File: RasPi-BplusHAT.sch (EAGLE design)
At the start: 1 part, among them K2 RASPI_HEADER

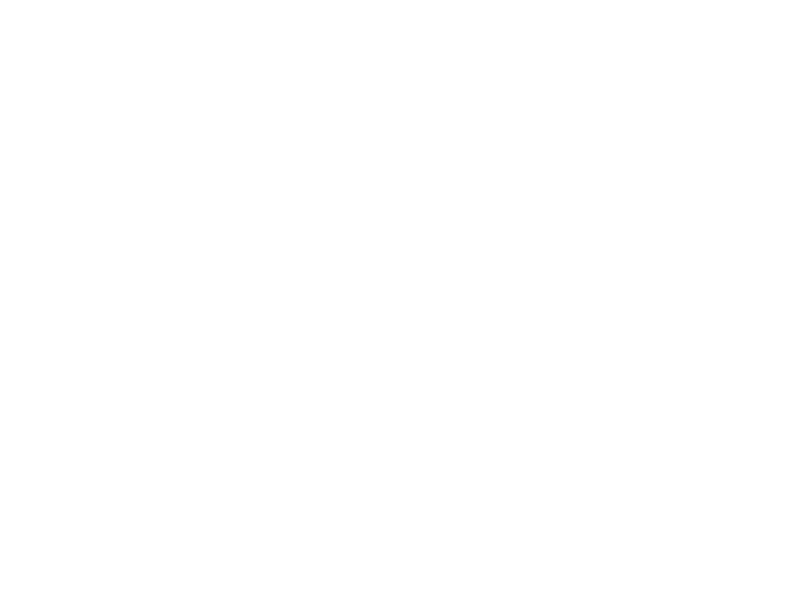
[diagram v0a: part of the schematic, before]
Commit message: add db15 and labeled nets
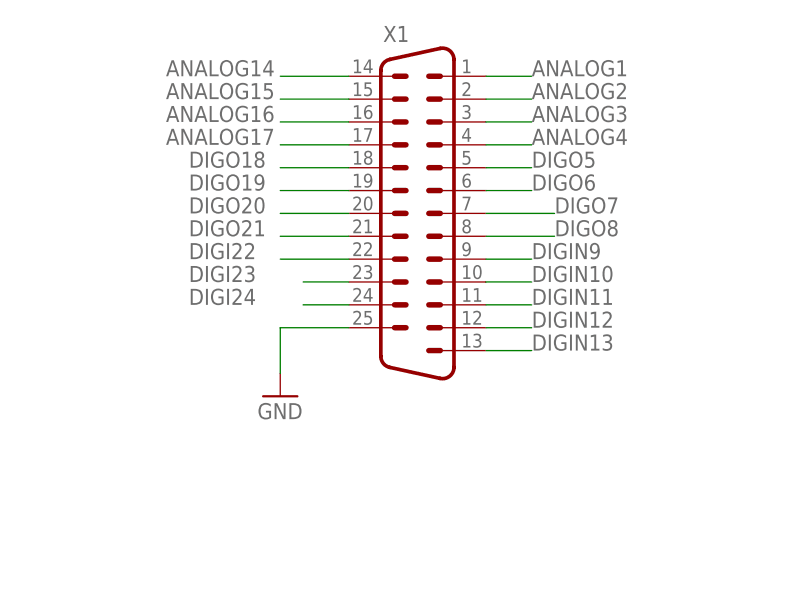
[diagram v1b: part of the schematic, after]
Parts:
- added X1: (no value), con-subd:M25HP
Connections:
- new net ANALOG1: X1G$1.1
- new net ANALOG14: X1G$1.14
- new net ANALOG15: X1G$1.15
- new net ANALOG16: X1G$1.16
- new net ANALOG17: X1G$1.17
- new net ANALOG2: X1G$1.2
- new net ANALOG3: X1G$1.3
- new net ANALOG4: X1G$1.4
- new net DIGI22: X1G$1.22
- new net DIGI23: X1G$1.23
- new net DIGI24: X1G$1.24
- new net DIGIN10: X1G$1.10
- new net DIGIN11: X1G$1.11
- new net DIGIN12: X1G$1.12
- new net DIGIN13: X1G$1.13
- new net DIGIN9: X1G$1.9
- new net DIGO18: X1G$1.18
- new net DIGO19: X1G$1.19
- new net DIGO20: X1G$1.20
- new net DIGO21: X1G$1.21
- new net DIGO5: X1G$1.5
- new net DIGO6: X1G$1.6
- new net DIGO7: X1G$1.7
- new net DIGO8: X1G$1.8
- net GND: now also X1G$1.25
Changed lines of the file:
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@@
 <part name="P+1" library="supply1" deviceset="+5V" device=""/>
 <part name="K2" library="RasPi-BplusHAT" deviceset="RASPI_HEADER" device=""/>
+<part name="X1" library="con-subd" deviceset="M25HP" device=""/>
+<part name="GND1" library="supply1" deviceset="GND" device=""/>
 </parts>
 <sheets>
@@
 </instance>
 <instance part="K2" gate="G$1" x="50.8" y="152.4" rot="R180"/>
+<instance part="X1" gate="G$1" x="177.8" y="187.96"/>
+<instance part="GND1" gate="1" x="162.56" y="165.1"/>
 </instances>
 <busses>
@@
 <pinref part="K2" gate="G$1" pin="34"/>
 </segment>
+<segment>
+<pinref part="X1" gate="G$1" pin="25"/>
+<wire x1="170.18" y1="172.72" x2="162.56" y2="172.72" width="0.1524" layer="91"/>
+<pinref part="GND1" gate="1" pin="GND"/>
+<wire x1="162.56" y1="172.72" x2="162.56" y2="167.64" width="0.1524" layer="91"/>
+</segment>
 </net>
 <net name="+3V3" class="0">
@@
 </segment>
 </net>
+<net name="ANALOG1" class="0">
+<segment>
+<pinref part="X1" gate="G$1" pin="1"/>
+<wire x1="185.42" y1="200.66" x2="190.5" y2="200.66" width="0.1524" layer="91"/>
+<label x="190.5" y="200.66" size="1.778" layer="95"/>
+</segment>
+</net>
+<net name="ANALOG2" class="0">
+<segment>
+<pinref part="X1" gate="G$1" pin="2"/>
+<wire x1="185.42" y1="198.12" x2="190.5" y2="198.12" width="0.1524" layer="91"/>
+<label x="190.5" y="198.12" size="1.778" layer="95"/>
+</segment>
+</net>
+<net name="ANALOG3" class="0">
+<segment>
+<pinref part="X1" gate="G$1" pin="3"/>
+<wire x1="185.42" y1="195.58" x2="190.5" y2="195.58" width="0.1524" layer="91"/>
+<label x="190.5" y="195.58" size="1.778" layer="95"/>
+</segment>
+</net>
+<net name="ANALOG4" class="0">
+<segment>
+<pinref part="X1" gate="G$1" pin="4"/>
+<wire x1="185.42" y1="193.04" x2="190.5" y2="193.04" width="0.1524" layer="91"/>
+<label x="190.5" y="193.04" size="1.778" layer="95"/>
+</segment>
+</net>
+<net name="DIGO5" class="0">
+<segment>
+<pinref part="X1" gate="G$1" pin="5"/>
+<wire x1="185.42" y1="190.5" x2="190.5" y2="190.5" width="0.1524" layer="91"/>
+<label x="190.5" y="190.5" size="1.778" layer="95"/>
+</segment>
+</net>
+<net name="DIGO6" class="0">
+<segment>
+<pinref part="X1" gate="G$1" pin="6"/>
+<wire x1="185.42" y1="187.96" x2="190.5" y2="187.96" width="0.1524" layer="91"/>
+<label x="190.5" y="187.96" size="1.778" layer="95"/>
+</segment>
+</net>
+<net name="DIGO7" class="0">
+<segment>
+<pinref part="X1" gate="G$1" pin="7"/>
+<wire x1="185.42" y1="185.42" x2="193.04" y2="185.42" width="0.1524" layer="91"/>
+<label x="193.04" y="185.42" size="1.778" layer="95"/>
+</segment>
+</net>
+<net name="DIGO8" class="0">
+<segment>
+<pinref part="X1" gate="G$1" pin="8"/>
+<wire x1="185.42" y1="182.88" x2="193.04" y2="182.88" width="0.1524" layer="91"/>
+<label x="193.04" y="182.88" size="1.778" layer="95"/>
+</segment>
+</net>
+<net name="DIGIN9" class="0">
+<segment>
+<pinref part="X1" gate="G$1" pin="9"/>
+<wire x1="185.42" y1="180.34" x2="190.5" y2="180.34" width="0.1524" layer="91"/>
+<label x="190.5" y="180.34" size="1.778" layer="95"/>
+</segment>
+</net>
+<net name="DIGIN10" class="0">
+<segment>
+<pinref part="X1" gate="G$1" pin="10"/>
+<wire x1="185.42" y1="177.8" x2="190.5" y2="177.8" width="0.1524" layer="91"/>
+<label x="190.5" y="177.8" size="1.778" layer="95"/>
+</segment>
+</net>
+<net name="DIGIN12" class="0">
+<segment>
+<pinref part="X1" gate="G$1" pin="12"/>
+<wire x1="185.42" y1="172.72" x2="190.5" y2="172.72" width="0.1524" layer="91"/>
+<label x="190.5" y="172.72" size="1.778" layer="95"/>
+</segment>
+</net>
+<net name="DIGIN13" class="0">
+<segment>
+<pinref part="X1" gate="G$1" pin="13"/>
+<wire x1="185.42" y1="170.18" x2="190.5" y2="170.18" width="0.1524" layer="91"/>
+<label x="190.5" y="170.18" size="1.778" layer="95"/>
+</segment>
+</net>
+<net name="ANALOG14" class="0">
+<segment>
+<pinref part="X1" gate="G$1" pin="14"/>
+<wire x1="170.18" y1="200.66" x2="162.56" y2="200.66" width="0.1524" layer="91"/>
+<label x="149.86" y="200.66" size="1.778" layer="95"/>
+</segment>
+</net>
+<net name="ANALOG15" class="0">
+<segment>
+<pinref part="X1" gate="G$1" pin="15"/>
+<wire x1="170.18" y1="198.12" x2="162.56" y2="198.12" width="0.1524" layer="91"/>
+<label x="149.86" y="198.12" size="1.778" layer="95"/>
+</segment>
+</net>
+<net name="ANALOG16" class="0">
+<segment>
+<pinref part="X1" gate="G$1" pin="16"/>
+<wire x1="170.18" y1="195.58" x2="162.56" y2="195.58" width="0.1524" layer="91"/>
+<label x="149.86" y="195.58" size="1.778" layer="95"/>
+</segment>
+</net>
+<net name="ANALOG17" class="0">
+<segment>
+<pinref part="X1" gate="G$1" pin="17"/>
+<wire x1="170.18" y1="193.04" x2="162.56" y2="193.04" width="0.1524" layer="91"/>
+<label x="149.86" y="193.04" size="1.778" layer="95"/>
+</segment>
+</net>
+<net name="DIGO18" class="0">
+<segment>
+<pinref part="X1" gate="G$1" pin="18"/>
+<wire x1="170.18" y1="190.5" x2="162.56" y2="190.5" width="0.1524" layer="91"/>
+<label x="152.4" y="190.5" size="1.778" layer="95"/>
+</segment>
+</net>
+<net name="DIGO19" class="0">
+<segment>
+<pinref part="X1" gate="G$1" pin="19"/>
+<wire x1="170.18" y1="187.96" x2="162.56" y2="187.96" width="0.1524" layer="91"/>
+<label x="152.4" y="187.96" size="1.778" layer="95"/>
+</segment>
+</net>
+<net name="DIGO20" class="0">
+<segment>
+<pinref part="X1" gate="G$1" pin="20"/>
+<wire x1="170.18" y1="185.42" x2="162.56" y2="185.42" width="0.1524" layer="91"/>
+<label x="152.4" y="185.42" size="1.778" layer="95"/>
+</segment>
+</net>
+<net name="DIGO21" class="0">
+<segment>
+<pinref part="X1" gate="G$1" pin="21"/>
+<wire x1="170.18" y1="182.88" x2="162.56" y2="182.88" width="0.1524" layer="91"/>
+<label x="152.4" y="182.88" size="1.778" layer="95"/>
+</segment>
+</net>
+<net name="DIGI22" class="0">
+<segment>
+<pinref part="X1" gate="G$1" pin="22"/>
+<wire x1="170.18" y1="180.34" x2="162.56" y2="180.34" width="0.1524" layer="91"/>
+<label x="152.4" y="180.34" size="1.778" layer="95"/>
+</segment>
+</net>
+<net name="DIGI23" class="0">
+<segment>
+<pinref part="X1" gate="G$1" pin="23"/>
+<wire x1="170.18" y1="177.8" x2="165.1" y2="177.8" width="0.1524" layer="91"/>
+<label x="152.4" y="177.8" size="1.778" layer="95"/>
+</segment>
+</net>
+<net name="DIGI24" class="0">
+<segment>
+<pinref part="X1" gate="G$1" pin="24"/>
+<wire x1="170.18" y1="175.26" x2="165.1" y2="175.26" width="0.1524" layer="91"/>
+<label x="152.4" y="175.26" size="1.778" layer="95"/>
+</segment>
+</net>
+<net name="DIGIN11" class="0">
+<segment>
+<pinref part="X1" gate="G$1" pin="11"/>
+<wire x1="185.42" y1="175.26" x2="190.5" y2="175.26" width="0.1524" layer="91"/>
+<label x="190.5" y="175.26" size="1.778" layer="95"/>
+</segment>
+</net>

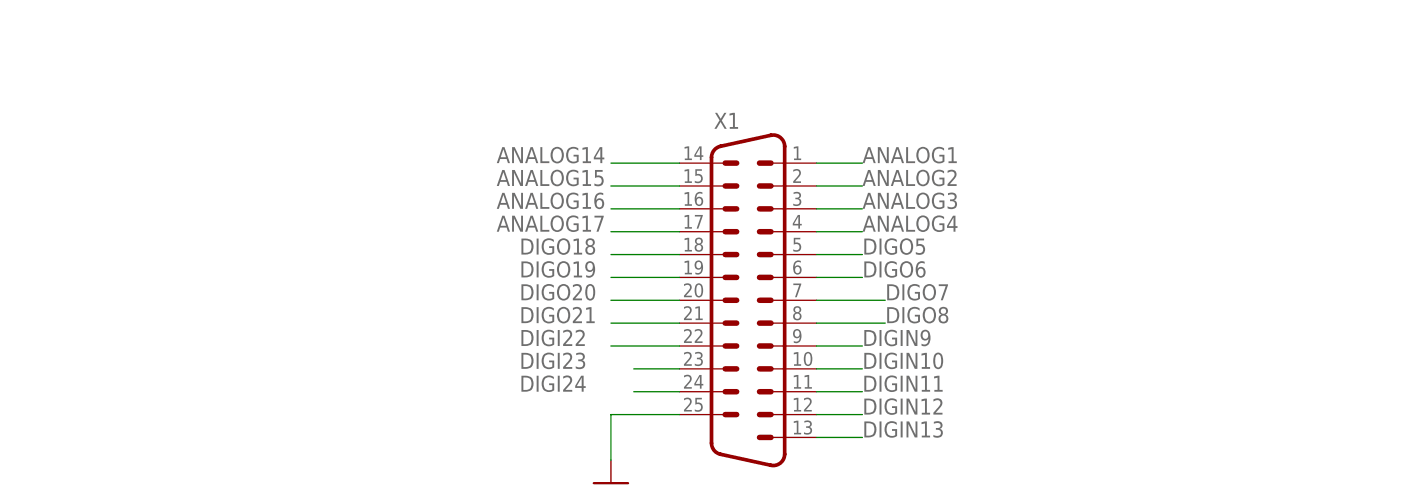
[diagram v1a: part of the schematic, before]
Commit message: add pullups
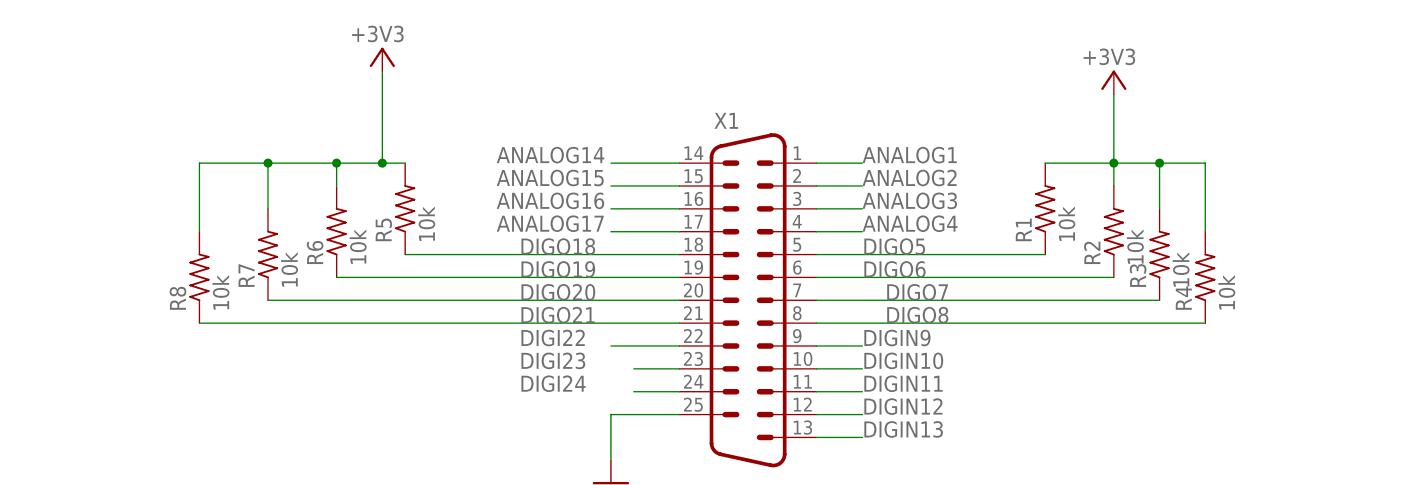
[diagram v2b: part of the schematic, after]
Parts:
- added R1, R2, R3, R4, R5, R6, R7, R8: 10k, resistor:R-US_0207/10
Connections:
- net +3V3: now also R1.2, R2.2, R3.2, R4.2, R5.2, R6.2, R7.2, R8.2
- net DIGO18: now also R5.1
- net DIGO19: now also R6.1
- net DIGO20: now also R7.1
- net DIGO21: now also R8.1
- net DIGO5: now also R1.1
- net DIGO6: now also R2.1
- net DIGO7: now also R3.1
- net DIGO8: now also R4.1
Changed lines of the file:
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@@
 <layer number="97" name="Info" color="7" fill="1" visible="yes" active="yes"/>
 <layer number="98" name="Guide" color="6" fill="1" visible="yes" active="yes"/>
+<layer number="99" name="SpiceOrder" color="5" fill="1" visible="yes" active="yes"/>
 <layer number="100" name="NonViaHole" color="7" fill="1" visible="yes" active="yes"/>
 <layer number="101" name="PlacementGuide" color="7" fill="1" visible="yes" active="yes"/>
@@
 <part name="X1" library="con-subd" deviceset="M25HP" device=""/>
 <part name="GND1" library="supply1" deviceset="GND" device=""/>
+<part name="+3V2" library="supply1" deviceset="+3V3" device=""/>
+<part name="R1" library="resistor" deviceset="R-US_" device="0207/10" value="10k"/>
+<part name="R2" library="resistor" deviceset="R-US_" device="0207/10" value="10k"/>
+<part name="R3" library="resistor" deviceset="R-US_" device="0207/10" value="10k"/>
+<part name="R4" library="resistor" deviceset="R-US_" device="0207/10" value="10k"/>
+<part name="+3V3" library="supply1" deviceset="+3V3" device=""/>
+<part name="R5" library="resistor" deviceset="R-US_" device="0207/10" value="10k"/>
+<part name="R6" library="resistor" deviceset="R-US_" device="0207/10" value="10k"/>
+<part name="R7" library="resistor" deviceset="R-US_" device="0207/10" value="10k"/>
+<part name="R8" library="resistor" deviceset="R-US_" device="0207/10" value="10k"/>
 </parts>
 <sheets>
@@
 <instance part="X1" gate="G$1" x="177.8" y="187.96"/>
 <instance part="GND1" gate="1" x="162.56" y="165.1"/>
+<instance part="+3V2" gate="G$1" x="218.44" y="210.82" smashed="yes">
+<attribute name="VALUE" x="220.98" y="213.36" size="1.778" layer="96" rot="R180"/>
+</instance>
+<instance part="R1" gate="G$1" x="210.82" y="195.58" rot="R90"/>
+<instance part="R2" gate="G$1" x="218.44" y="193.04" rot="R90"/>
+<instance part="R3" gate="G$1" x="223.52" y="190.5" rot="R90"/>
+<instance part="R4" gate="G$1" x="228.6" y="187.96" rot="R90"/>
+<instance part="+3V3" gate="G$1" x="137.16" y="213.36" smashed="yes">
+<attribute name="VALUE" x="139.7" y="215.9" size="1.778" layer="96" rot="R180"/>
+</instance>
+<instance part="R5" gate="G$1" x="139.7" y="195.58" rot="R90"/>
+<instance part="R6" gate="G$1" x="132.08" y="193.04" rot="R90"/>
+<instance part="R7" gate="G$1" x="124.46" y="190.5" rot="R90"/>
+<instance part="R8" gate="G$1" x="116.84" y="187.96" rot="R90"/>
 </instances>
 <busses>
@@
 <pinref part="K2" gate="G$1" pin="17"/>
 </segment>
+<segment>
+<pinref part="R1" gate="G$1" pin="2"/>
+<pinref part="+3V2" gate="G$1" pin="+3V3"/>
+<wire x1="210.82" y1="200.66" x2="218.44" y2="200.66" width="0.1524" layer="91"/>
+<wire x1="218.44" y1="200.66" x2="218.44" y2="208.28" width="0.1524" layer="91"/>
+<pinref part="R2" gate="G$1" pin="2"/>
+<wire x1="218.44" y1="198.12" x2="218.44" y2="200.66" width="0.1524" layer="91"/>
+<junction x="218.44" y="200.66"/>
+<pinref part="R3" gate="G$1" pin="2"/>
+<wire x1="218.44" y1="200.66" x2="223.52" y2="200.66" width="0.1524" layer="91"/>
+<wire x1="223.52" y1="200.66" x2="223.52" y2="195.58" width="0.1524" layer="91"/>
+<pinref part="R4" gate="G$1" pin="2"/>
+<wire x1="223.52" y1="200.66" x2="228.6" y2="200.66" width="0.1524" layer="91"/>
+<wire x1="228.6" y1="200.66" x2="228.6" y2="193.04" width="0.1524" layer="91"/>
+<junction x="223.52" y="200.66"/>
+</segment>
+<segment>
+<pinref part="R5" gate="G$1" pin="2"/>
+<pinref part="+3V3" gate="G$1" pin="+3V3"/>
+<wire x1="139.7" y1="200.66" x2="137.16" y2="200.66" width="0.1524" layer="91"/>
+<wire x1="137.16" y1="200.66" x2="137.16" y2="210.82" width="0.1524" layer="91"/>
+<pinref part="R6" gate="G$1" pin="2"/>
+<wire x1="132.08" y1="198.12" x2="132.08" y2="200.66" width="0.1524" layer="91"/>
+<wire x1="132.08" y1="200.66" x2="137.16" y2="200.66" width="0.1524" layer="91"/>
+<junction x="137.16" y="200.66"/>
+<pinref part="R7" gate="G$1" pin="2"/>
+<wire x1="124.46" y1="195.58" x2="124.46" y2="200.66" width="0.1524" layer="91"/>
+<wire x1="124.46" y1="200.66" x2="132.08" y2="200.66" width="0.1524" layer="91"/>
+<junction x="132.08" y="200.66"/>
+<pinref part="R8" gate="G$1" pin="2"/>
+<wire x1="116.84" y1="193.04" x2="116.84" y2="200.66" width="0.1524" layer="91"/>
+<wire x1="116.84" y1="200.66" x2="124.46" y2="200.66" width="0.1524" layer="91"/>
+<junction x="124.46" y="200.66"/>
+</segment>
 </net>
 <net name="+5V" class="0">
@@
 <segment>
 <pinref part="X1" gate="G$1" pin="5"/>
-<wire x1="185.42" y1="190.5" x2="190.5" y2="190.5" width="0.1524" layer="91"/>
 <label x="190.5" y="190.5" size="1.778" layer="95"/>
+<pinref part="R1" gate="G$1" pin="1"/>
+<wire x1="185.42" y1="190.5" x2="210.82" y2="190.5" width="0.1524" layer="91"/>
 </segment>
 </net>
@@
 <segment>
 <pinref part="X1" gate="G$1" pin="6"/>
-<wire x1="185.42" y1="187.96" x2="190.5" y2="187.96" width="0.1524" layer="91"/>
 <label x="190.5" y="187.96" size="1.778" layer="95"/>
+<wire x1="185.42" y1="187.96" x2="218.44" y2="187.96" width="0.1524" layer="91"/>
+<pinref part="R2" gate="G$1" pin="1"/>
 </segment>
 </net>
@@
 <segment>
 <pinref part="X1" gate="G$1" pin="7"/>
-<wire x1="185.42" y1="185.42" x2="193.04" y2="185.42" width="0.1524" layer="91"/>
 <label x="193.04" y="185.42" size="1.778" layer="95"/>
+<wire x1="185.42" y1="185.42" x2="223.52" y2="185.42" width="0.1524" layer="91"/>
+<pinref part="R3" gate="G$1" pin="1"/>
 </segment>
 </net>
@@
 <segment>
 <pinref part="X1" gate="G$1" pin="8"/>
-<wire x1="185.42" y1="182.88" x2="193.04" y2="182.88" width="0.1524" layer="91"/>
 <label x="193.04" y="182.88" size="1.778" layer="95"/>
+<wire x1="185.42" y1="182.88" x2="228.6" y2="182.88" width="0.1524" layer="91"/>
+<pinref part="R4" gate="G$1" pin="1"/>
 </segment>
 </net>
@@
 <segment>
 <pinref part="X1" gate="G$1" pin="18"/>
-<wire x1="170.18" y1="190.5" x2="162.56" y2="190.5" width="0.1524" layer="91"/>
 <label x="152.4" y="190.5" size="1.778" layer="95"/>
+<wire x1="170.18" y1="190.5" x2="139.7" y2="190.5" width="0.1524" layer="91"/>
+<pinref part="R5" gate="G$1" pin="1"/>
 </segment>
 </net>
@@
 <segment>
 <pinref part="X1" gate="G$1" pin="19"/>
-<wire x1="170.18" y1="187.96" x2="162.56" y2="187.96" width="0.1524" layer="91"/>
 <label x="152.4" y="187.96" size="1.778" layer="95"/>
+<wire x1="170.18" y1="187.96" x2="132.08" y2="187.96" width="0.1524" layer="91"/>
+<pinref part="R6" gate="G$1" pin="1"/>
 </segment>
 </net>
@@
 <segment>
 <pinref part="X1" gate="G$1" pin="20"/>
-<wire x1="170.18" y1="185.42" x2="162.56" y2="185.42" width="0.1524" layer="91"/>
 <label x="152.4" y="185.42" size="1.778" layer="95"/>
+<wire x1="170.18" y1="185.42" x2="124.46" y2="185.42" width="0.1524" layer="91"/>
+<pinref part="R7" gate="G$1" pin="1"/>
 </segment>
 </net>
@@
 <segment>
 <pinref part="X1" gate="G$1" pin="21"/>
-<wire x1="170.18" y1="182.88" x2="162.56" y2="182.88" width="0.1524" layer="91"/>
 <label x="152.4" y="182.88" size="1.778" layer="95"/>
-</segment>
-</net>
+<wire x1="170.18" y1="182.88" x2="116.84" y2="182.88" width="0.1524" layer="91"/>
+<pinref part="R8" gate="G$1" pin="1"/>
+</segment>
+</net>
